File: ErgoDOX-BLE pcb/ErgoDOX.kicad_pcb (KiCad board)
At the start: 2 copper layers, 182.8 x 158.9 mm, 110 parts, among them J1 Conn_01x04, J2 Conn_01x02_Female, J3 Conn_01x02_Female, J4 Conn_01x02, J5 Conn_01x02, P1 USB_C_Plug_USB2.0, Q1 Q_NPN_BCE, SW0:10 SW0:3, SW0:11 SW0:2, SW0:12 SW0:1, SW0:7 SW0:6, SW0:8 SW0:5, SW0:9 SW0:4, SW1:10 SW1:3, SW1:11 SW1:2, SW1:12 SW1:1, SW1:13 SW1:0, SW1:9 SW1:4, SW2:10 SW2:3, SW2:11 SW2:2, SW2:12 SW2:1, SW2:13 SW2:0, SW2:7 SW2:6, SW2:8 SW2:5, SW2:9 SW2:4, SW3:10 SW3:3, SW3:11 SW3:2, SW3:12 SW3:1, SW3:13 SW3:0, SW3:8 SW3:5, SW3:9 SW3:4, SW4:10 SW4:3, SW4:11 SW4:2, SW4:12 SW4:1, SW4:13 SW4:0, SW4:7 SW4:6, SW4:8 SW4:5, SW4:9 SW4:4, SW5:10 SW5:3, SW5:11 SW5:2, SW5:12 SW5:1, SW5:13 SW5:0, SW5:7 SW5:6, SW5:8 SW5:5, SW5:9 SW5:4, U1 MCP23018, U3 C0720B001F

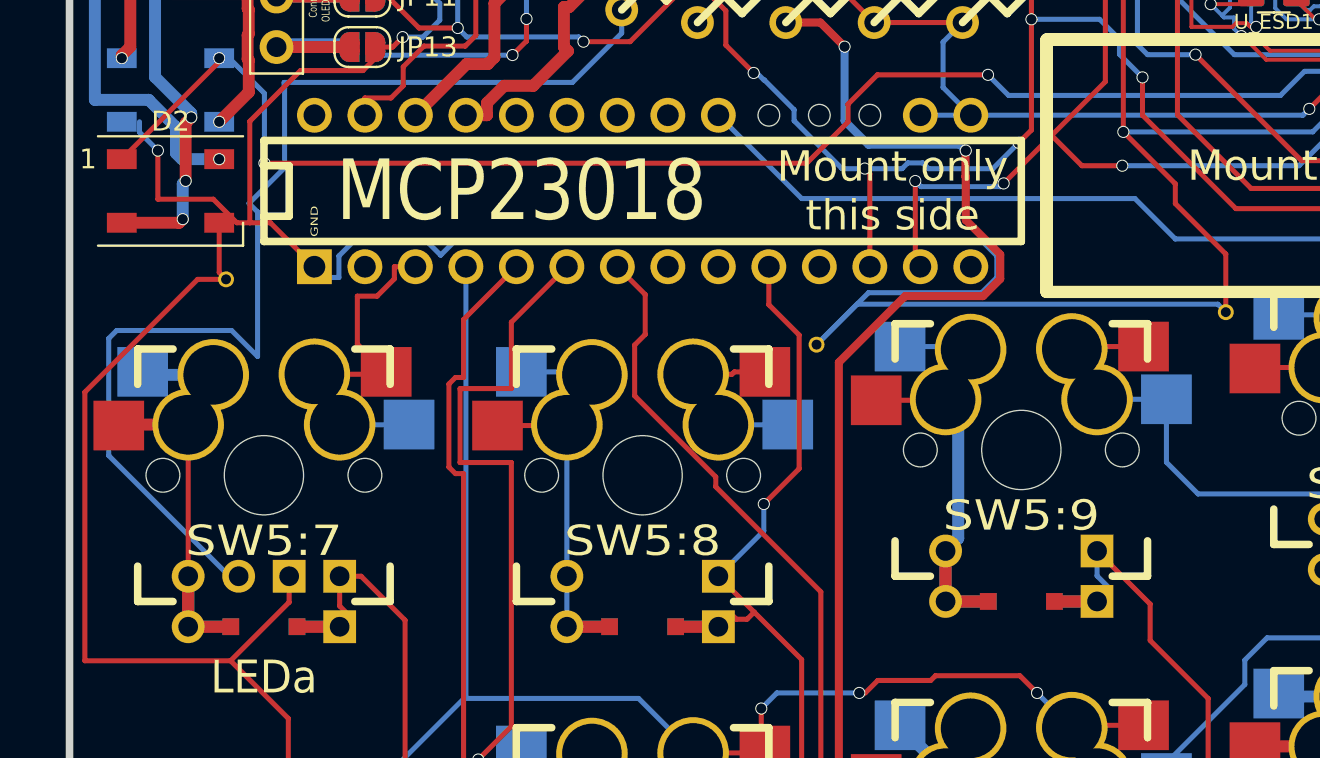
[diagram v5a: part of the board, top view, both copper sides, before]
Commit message: Connect a missing trace
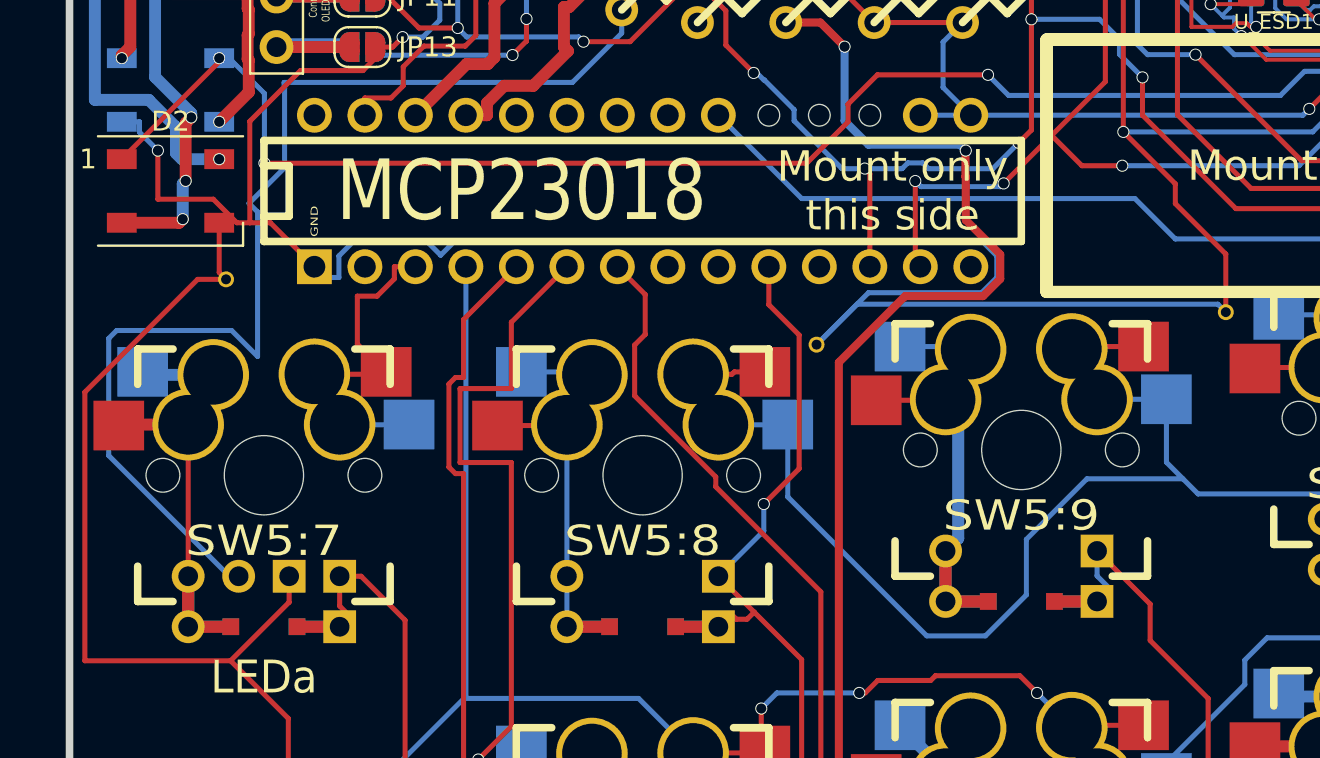
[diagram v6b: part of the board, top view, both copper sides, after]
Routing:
- net /ROW5: track 191.1 -> 222.4 mm
- net GND: track 660.8 -> 661.7 mm
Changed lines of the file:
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@@
   (segment (start 193.9925 61.9252) (end 195.2625 63.1952) (width 0.254) (layer "B.Cu") (net 14))
   (segment (start 171.45 66.548161) (end 171.45 64.4652) (width 0.254) (layer "B.Cu") (net 14))
+  (segment (start 105.732899 73.179364) (end 108.684636 73.179364) (width 0.254) (layer "B.Cu") (net 14))
   (segment (start 170.3578 62.103) (end 179.5018 62.103) (width 0.254) (layer "B.Cu") (net 14))
+  (segment (start 119.38 66.04) (end 118.618 65.278) (width 0.254) (layer "B.Cu") (net 14))
+  (segment (start 108.684636 73.179364) (end 110.744 71.12) (width 0.254) (layer "B.Cu") (net 14))
   (segment (start 144.78 73.66) (end 154.94 73.66) (width 0.254) (layer "B.Cu") (net 14))
   (segment (start 117.79 61.27766) (end 114.31 61.27766) (width 0.254) (layer "B.Cu") (net 14))
@@
   (segment (start 76.2 62.5602) (end 79.65 62.5602) (width 0.254) (layer "B.Cu") (net 14))
   (segment (start 137.16 66.04) (end 144.78 73.66) (width 0.254) (layer "B.Cu") (net 14))
+  (segment (start 98.74 62.5502) (end 98.74 66.186465) (width 0.254) (layer "B.Cu") (net 14))
   (segment (start 181.9148 59.69) (end 191.7573 59.69) (width 0.254) (layer "B.Cu") (net 14))
   (segment (start 174.94 64.4552) (end 171.46 64.4552) (width 0.254) (layer "B.Cu") (net 14))
@@
   (segment (start 133.36 59.68) (end 133.35 59.69) (width 0.254) (layer "B.Cu") (net 14))
   (segment (start 114.31 61.27766) (end 114.3 61.28766) (width 0.254) (layer "B.Cu") (net 14))
+  (segment (start 98.74 66.186465) (end 105.732899 73.179364) (width 0.254) (layer "B.Cu") (net 14))
   (segment (start 155.89 70.927) (end 155.9891 70.8279) (width 0.254) (layer "B.Cu") (net 14))
   (segment (start 117.79 64.45) (end 117.79 61.27766) (width 0.254) (layer "B.Cu") (net 14))
@@
   (segment (start 195.2725 64.4552) (end 195.2625 64.4652) (width 0.254) (layer "B.Cu") (net 14))
   (segment (start 136.84 59.68) (end 136.84 65.72) (width 0.254) (layer "B.Cu") (net 14))
+  (segment (start 118.618 65.278) (end 117.79 64.45) (width 0.254) (layer "B.Cu") (net 14))
   (segment (start 155.89 72.71) (end 155.89 70.927) (width 0.254) (layer "B.Cu") (net 14))
   (segment (start 167.170261 70.8279) (end 171.45 66.548161) (width 0.254) (layer "B.Cu") (net 14))
   (segment (start 136.84 59.68) (end 133.36 59.68) (width 0.254) (layer "B.Cu") (net 14))
+  (segment (start 110.744 68.326) (end 113.792 65.278) (width 0.254) (layer "B.Cu") (net 14))
   (segment (start 154.94 73.66) (end 155.89 72.71) (width 0.254) (layer "B.Cu") (net 14))
   (segment (start 98.73 62.5602) (end 98.74 62.5502) (width 0.254) (layer "B.Cu") (net 14))
@@
   (segment (start 156.0272 70.866) (end 156.591 70.866) (width 0.254) (layer "B.Cu") (net 14))
   (segment (start 155.89 61.27766) (end 152.41 61.27766) (width 0.254) (layer "B.Cu") (net 14))
+  (segment (start 110.744 71.12) (end 110.744 68.326) (width 0.254) (layer "B.Cu") (net 14))
   (segment (start 151.13 58.74766) (end 152.4 60.01766) (width 0.254) (layer "B.Cu") (net 14))
-  (segment (start 119.38 66.04) (end 117.79 64.45) (width 0.254) (layer "B.Cu") (net 14))
   (segment (start 155.89 70.927) (end 155.89 61.27766) (width 0.254) (layer "B.Cu") (net 14))
+  (segment (start 113.792 65.278) (end 118.618 65.278) (width 0.254) (layer "B.Cu") (net 14))
   (segment (start 155.9891 70.8279) (end 156.0272 70.866) (width 0.254) (layer "B.Cu") (net 14))
   (segment (start 74.93 60.0202) (end 76.2 61.2902) (width 0.254) (layer "B.Cu") (net 14))
@@
   (segment (start 134.693 36.537) (end 133.638 37.592) (width 0.254) (layer "B.Cu") (net 15))
   (segment (start 151.439 33.909) (end 150.564001 34.783999) (width 0.254) (layer "B.Cu") (net 15))
+  (segment (start 66.13 47.32) (end 65.241 47.32) (width 0.254) (layer "B.Cu") (net 15))
   (segment (start 120.142 40.386) (end 120.269 40.386) (width 0.254) (layer "B.Cu") (net 15))
   (segment (start 204.724 48.768) (end 204.724 55.118) (width 0.254) (layer "B.Cu") (net 15))

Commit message: Route me daddy
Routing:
- net /ROW0: track 139.8 -> 243.9 mm, vias 0 -> 1
- net /COL6: track 116.4 -> 175.9 mm
- net /COL3: track 92.1 -> 143.1 mm
- net /ROW4: track 255.8 -> 206.9 mm, vias 3 -> 5
- net /ROW5: track 222.4 -> 263.1 mm, vias 2 -> 3
- net /ROW1: track 218.1 -> 224.0 mm
- net Net-(LED_A1-Pad1): track 57.0 -> 62.4 mm
- net GND: track 661.7 -> 666.6 mm, vias 14 -> 15
- net /COL5: track 218.9 -> 222.0 mm
- net /COL1: track 250.7 -> 249.6 mm
- net /COL2: track 179.1 -> 178.0 mm

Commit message: Everything is connected
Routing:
- net +3V3: track 135.0 -> 304.2 mm, vias 6 -> 7
- net /COL1: track 249.6 -> 349.8 mm, vias 0 -> 1
- net /COL2: track 178.0 -> 258.2 mm
- net Net-(LED_B1-Pad1): track 0.00 -> 78.4 mm, vias 0 -> 2
- net /COL3: track 143.1 -> 212.0 mm, vias 1 -> 2
- net /COL4: track 240.6 -> 287.3 mm, vias 2 -> 3
- net GND: track 666.6 -> 695.8 mm, vias 15 -> 16
- net /SDA: track 194.5 -> 202.3 mm, vias 7 -> 5
- net /ROW5: track 263.1 -> 269.6 mm, vias 3 -> 4
- net /ROW0: track 243.9 -> 241.2 mm
- net /ROW4: track 206.9 -> 205.3 mm
- net /COL0: track 231.0 -> 231.9 mm
- net +5V: track 180.2 -> 181.1 mm
